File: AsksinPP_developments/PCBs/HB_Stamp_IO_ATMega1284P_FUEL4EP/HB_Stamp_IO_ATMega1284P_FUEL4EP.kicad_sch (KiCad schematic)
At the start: 35 parts, among them J1 Power, J2 FTDI Debuger, J3 ISP Programmer, J4 IO1, J5 IO2, J6 IO3, U1 ATmega1284P-AU, U2 TPS61221DCK

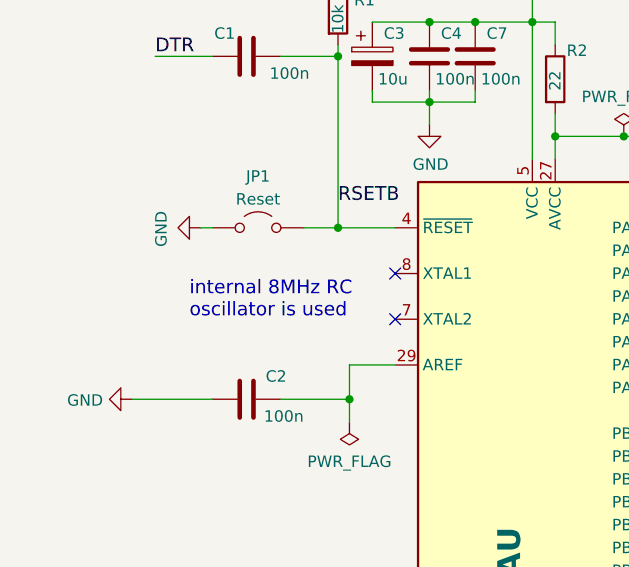
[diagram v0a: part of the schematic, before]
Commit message: PCBs/HB_Stamp_IO_ATMega1284P_FUEL4EP: added test point TP3 (XTAL1)
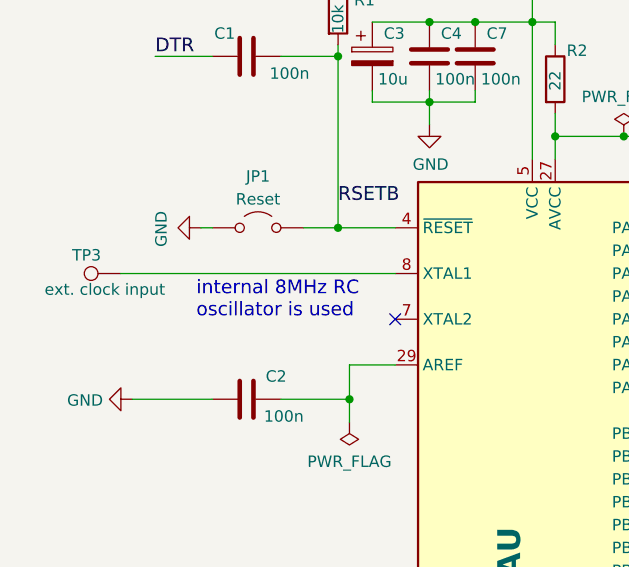
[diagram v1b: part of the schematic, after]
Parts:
- added TP3: ext. clock input, TestPoint:TestPoint_Pad_1.0x1.0mm, symbol Connector:TestPoint
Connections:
- net at U1.8 (XTAL1): now also TP3.1
- no-connect marks 13 -> 12
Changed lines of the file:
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@@
 	(title_block
 		(title "HB_Stamp_IO_ATMega1284P_FUEL4EP")
-		(date "2025-02-17")
-		(rev "1.0")
+		(date "2025-05-09")
+		(rev "1.1")
 		(company "(C) FUEL4EP")
 		(comment 1 "Creative Commons License, non-commercial")
@@
 	)
 	(no_connect
-		(at 52.07 96.52)
-	)
-	(no_connect
 		(at 82.55 167.64)
 	)
@@
 	(wire
 		(pts
+			(xy 21.59 96.52) (xy 52.07 96.52)
+		)
+		(stroke
+			(width 0)
+			(type default)
+		)
+	)
+	(wire
+		(pts
 			(xy 67.31 189.23) (xy 72.39 189.23)
 		)
@@
 	(text "internal 8MHz RC\noscillator is used"
 		(exclude_from_sim no)
-		(at 29.21 101.6 0)
+		(at 29.972 101.6 0)
 		(effects
 			(font
@@
 					(unit 1)
 				)
+			)
+		)
+	)
+	(symbol
+		(lib_id "Connector:TestPoint")
+		(at 21.59 96.52 90)
+		(unit 1)
+		(exclude_from_sim no)
+		(in_bom yes)
+		(on_board yes)
+		(dnp no)
+		(property "Reference" "TP3"
+			(at 17.78 94.488 90)
+			(effects
+				(font
+					(size 1.27 1.27)
+				)
+			)
+		)
+		(property "Value" "ext. clock input"
+			(at 19.812 98.298 90)
+			(effects
+				(font
+					(size 1.27 1.27)
+				)
+			)
+		)
+		(property "Footprint" "TestPoint:TestPoint_Pad_1.0x1.0mm"
+			(at 21.59 91.44 0)
+			(effects
+				(font
+					(size 1.27 1.27)
+				)
+				(hide yes)
+			)
+		)
+		(property "Datasheet" "~"
+			(at 21.59 91.44 0)
+			(effects
+				(font
+					(size 1.27 1.27)
+				)
+				(hide yes)
+			)
+		)
+		(property "Description" "test point"
+			(at 21.59 96.52 0)
+			(effects
+				(font
+					(size 1.27 1.27)
+				)
+				(hide yes)
+			)
+		)
+		(property "Sim.Enable" ""
+			(at 21.59 96.52 0)
+			(effects
+				(font
+					(size 1.27 1.27)
+				)
+				(hide yes)
+			)
+		)
+		(pin "1"
+		)
+		(instances
+			(project "HB_Stamp_IO_ATMega1284P_FUEL4EP"
+				(path "/7766ca2c-d652-431b-ba34-0d354b09e90f"
+					(reference "TP3")
+					(unit 1)
+				)
